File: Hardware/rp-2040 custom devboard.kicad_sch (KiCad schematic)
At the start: 36 parts, among them J1 USB_C_Receptacle_USB2.0_14P, J2 Conn_01x20, J3 Conn_01x20, J4 Conn_01x03, SW1 SW_Push, U1 RP2040, U2 MCP1700x-330xxTT, U3 W25Q128JVS, U4 SK6812MINI-E, Y1 12 MHz

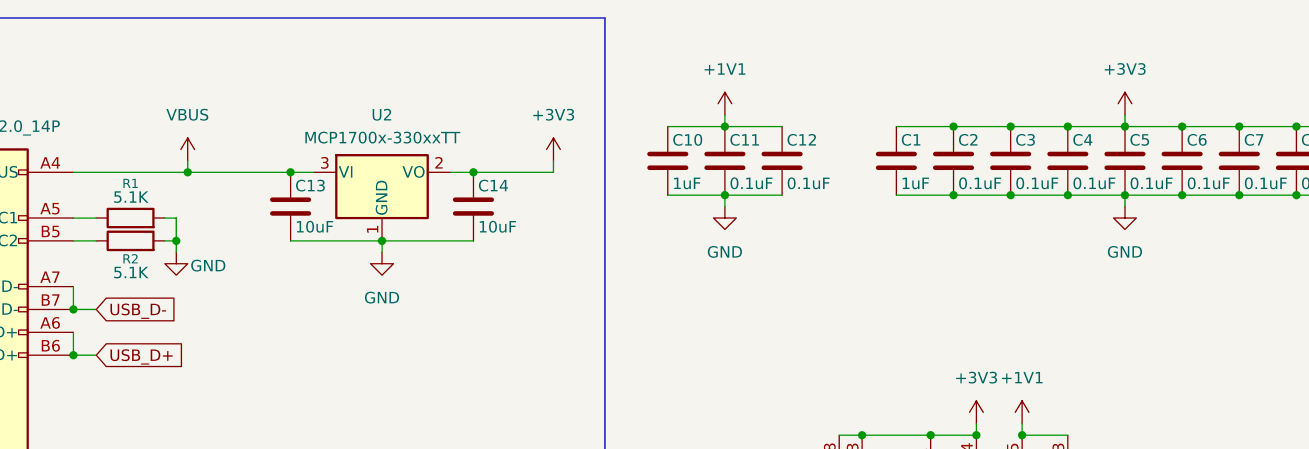
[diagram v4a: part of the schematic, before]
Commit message: learnt what PWR_FLAGs are and used them to get 0 ERC errors, lets go ahead with the footprints
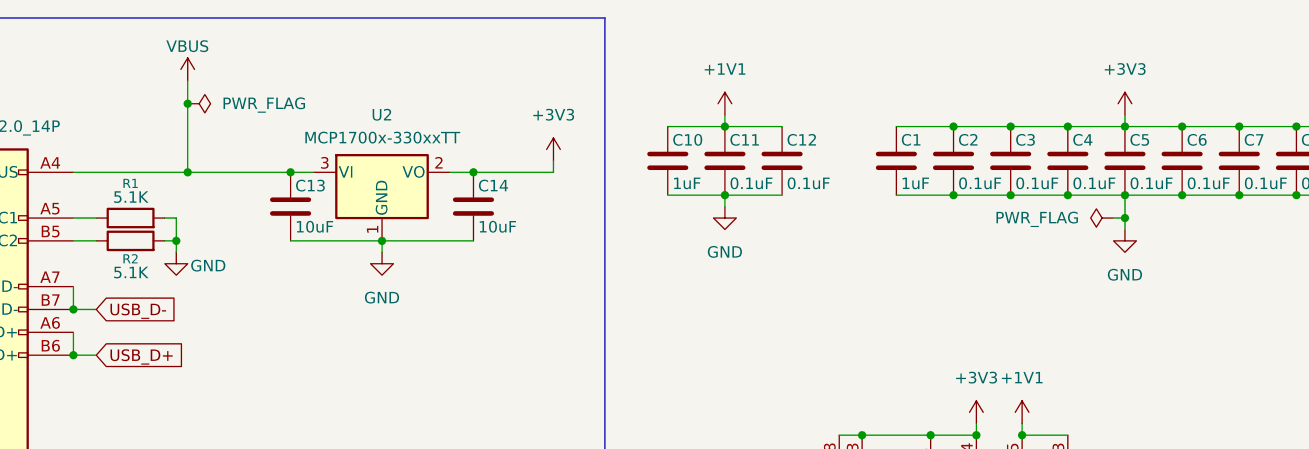
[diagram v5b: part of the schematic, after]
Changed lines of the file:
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@@
 	)
 	(junction
+		(at 64.77 25.4)
+		(diameter 0)
+		(color 0 0 0 0)
+	)
+	(junction
 		(at 256.54 43.18)
 		(diameter 0)
@@
 	)
 	(junction
+		(at 168.91 38.1)
+		(diameter 0)
+		(color 0 0 0 0)
+	)
+	(junction
 		(at 241.3 132.08)
 		(diameter 0)
@@
 	(wire
 		(pts
+			(xy 167.64 38.1) (xy 168.91 38.1)
+		)
+		(stroke
+			(width 0)
+			(type default)
+		)
+	)
+	(wire
+		(pts
 			(xy 80.01 163.83) (xy 80.01 176.53)
 		)
@@
 	(wire
 		(pts
-			(xy 64.77 31.75) (xy 64.77 33.02)
-		)
-		(stroke
-			(width 0)
-			(type default)
-		)
-	)
-	(wire
-		(pts
 			(xy 78.74 158.75) (xy 82.55 158.75)
 		)
@@
 	(wire
 		(pts
+			(xy 168.91 39.37) (xy 168.91 38.1)
+		)
+		(stroke
+			(width 0)
+			(type default)
+		)
+	)
+	(wire
+		(pts
 			(xy 168.91 26.67) (xy 168.91 27.94)
 		)
@@
 	(wire
 		(pts
+			(xy 64.77 25.4) (xy 64.77 33.02)
+		)
+		(stroke
+			(width 0)
+			(type default)
+		)
+	)
+	(wire
+		(pts
 			(xy 66.04 105.41) (xy 66.04 107.95)
 		)
@@
 	(wire
 		(pts
+			(xy 168.91 35.56) (xy 168.91 38.1)
+		)
+		(stroke
+			(width 0)
+			(type default)
+		)
+	)
+	(wire
+		(pts
 			(xy 175.26 146.05) (xy 176.53 146.05)
 		)
@@
 	(wire
 		(pts
-			(xy 168.91 35.56) (xy 168.91 36.83)
-		)
-		(stroke
-			(width 0)
-			(type default)
-		)
-	)
-	(wire
-		(pts
 			(xy 78.74 161.29) (xy 82.55 161.29)
 		)
@@
 	(wire
 		(pts
+			(xy 64.77 22.86) (xy 64.77 25.4)
+		)
+		(stroke
+			(width 0)
+			(type default)
+		)
+	)
+	(wire
+		(pts
 			(xy 139.7 62.23) (xy 147.32 62.23)
 		)
@@
 	)
 	(symbol
+		(lib_id "power:PWR_FLAG")
+		(at 64.77 25.4 270)
+		(unit 1)
+		(exclude_from_sim no)
+		(in_bom yes)
+		(on_board yes)
+		(dnp no)
+		(property "Reference" "#FLG02"
+			(at 66.675 25.4 0)
+			(effects
+				(font
+					(size 1.27 1.27)
+				)
+				(hide yes)
+			)
+		)
+		(property "Value" "PWR_FLAG"
+			(at 68.58 25.4001 90)
+			(effects
+				(font
+					(size 1.27 1.27)
+				)
+				(justify left)
+			)
+		)
+		(property "Footprint" ""
+			(at 64.77 25.4 0)
+			(effects
+				(font
+					(size 1.27 1.27)
+				)
+				(hide yes)
+			)
+		)
+		(property "Datasheet" "~"
+			(at 64.77 25.4 0)
+			(effects
+				(font
+					(size 1.27 1.27)
+				)
+				(hide yes)
+			)
+		)
+		(property "Description" "Special symbol for telling ERC where power comes from"
+			(at 64.77 25.4 0)
+			(effects
+				(font
+					(size 1.27 1.27)
+				)
+				(hide yes)
+			)
+		)
+		(pin "1"
+		)
+		(instances
+			(project ""
+				(path "/6a6cd6ef-7cbc-401d-a6e8-493482b4d165"
+					(reference "#FLG02")
+					(unit 1)
+				)
+			)
+		)
+	)
+	(symbol
 		(lib_id "Device:C")
 		(at 118.11 31.75 0)
@@
 	(symbol
 		(lib_id "power:GND")
-		(at 168.91 36.83 0)
+		(at 168.91 39.37 0)
 		(unit 1)
 		(exclude_from_sim no)
@@
 		(fields_autoplaced yes)
 		(property "Reference" "#PWR04"
-			(at 168.91 43.18 0)
+			(at 168.91 45.72 0)
 			(effects
 				(font
@@
 		)
 		(property "Value" "GND"
-			(at 168.91 41.91 0)
+			(at 168.91 44.45 0)
 			(effects
 				(font
@@
 		)
 		(property "Footprint" ""
-			(at 168.91 36.83 0)
+			(at 168.91 39.37 0)
 			(effects
 				(font
@@
 		)
 		(property "Datasheet" ""
-			(at 168.91 36.83 0)
+			(at 168.91 39.37 0)
 			(effects
 				(font
@@
 		)
 		(property "Description" "Power symbol creates a global label with name \"GND\" , ground"
-			(at 168.91 36.83 0)
+			(at 168.91 39.37 0)
 			(effects
 				(font
@@
 	(symbol
 		(lib_id "power:VBUS")
-		(at 64.77 31.75 0)
+		(at 64.77 22.86 0)
 		(unit 1)
 		(exclude_from_sim no)
@@
 		(fields_autoplaced yes)
 		(property "Reference" "#PWR010"
-			(at 64.77 35.56 0)
+			(at 64.77 26.67 0)
 			(effects
 				(font
@@
 		)
 		(property "Value" "VBUS"
-			(at 64.77 26.67 0)
+			(at 64.77 19.05 0)
 			(effects
 				(font
@@
 		)
 		(property "Footprint" ""
-			(at 64.77 31.75 0)
+			(at 64.77 22.86 0)
 			(effects
 				(font
@@
 		)
 		(property "Datasheet" ""
-			(at 64.77 31.75 0)
+			(at 64.77 22.86 0)
 			(effects
 				(font
@@
 		)
 		(property "Description" "Power symbol creates a global label with name \"VBUS\""
-			(at 64.77 31.75 0)
+			(at 64.77 22.86 0)
 			(effects
 				(font
@@
 					(unit 1)
 				)
+			)
+		)
+	)
+	(symbol
+		(lib_id "power:PWR_FLAG")
+		(at 167.64 38.1 90)
+		(unit 1)
+		(exclude_from_sim no)
+		(in_bom yes)
+		(on_board yes)
+		(dnp no)
+		(fields_autoplaced yes)
+		(property "Reference" "#FLG01"
+			(at 165.735 38.1 0)
+			(effects
+				(font
+					(size 1.27 1.27)
+				)
+				(hide yes)
+			)
+		)
+		(property "Value" "PWR_FLAG"
+			(at 163.83 38.0999 90)
+			(effects
+				(font
+					(size 1.27 1.27)
+				)
+				(justify left)
+			)
+		)
+		(property "Footprint" ""
+			(at 167.64 38.1 0)
+			(effects
+				(font
+					(size 1.27 1.27)
+				)
+				(hide yes)
+			)
+		)
+		(property "Datasheet" "~"
+			(at 167.64 38.1 0)
+			(effects
+				(font
+					(size 1.27 1.27)
+				)
+				(hide yes)
+			)
+		)
+		(property "Description" "Special symbol for telling ERC where power comes from"
+			(at 167.64 38.1 0)
+			(effects
+				(font
+					(size 1.27 1.27)
+				)
+				(hide yes)
+			)
+		)
+		(pin "1"
+		)
+		(instances
+			(project ""
+				(path "/6a6cd6ef-7cbc-401d-a6e8-493482b4d165"
+					(reference "#FLG01")
+					(unit 1)
+				)

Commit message: couldnt find the footprint for the SK6812MINI-E but i downloaded it again and it worked this time
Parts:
- C1, C10, C11, C12, C15, C16, C17, C2, C3, C4, C5, C6, C7, C8, C9: footprint (none) -> Capacitor_SMD:C_0402_1005Metric
- C13, C14: footprint (none) -> Capacitor_SMD:C_0603_1608Metric
- C19: value 100nF -> 0.1uF; footprint (none) -> Capacitor_SMD:C_0402_1005Metric
- J1: footprint (none) -> Connector_USB:USB_C_Receptacle_HRO_TYPE-C-31-M-12
- J2, J3: footprint (none) -> Connector_PinHeader_2.54mm:PinHeader_1x20_P2.54mm_Vertical
- J4: footprint (none) -> Connector_PinHeader_2.54mm:PinHeader_1x03_P2.54mm_Vertical
- R1, R2, R3, R4, R5, R6, R7, R9: footprint (none) -> Resistor_SMD:R_0402_1005Metric
- SW1: footprint (none) -> Button_Switch_SMD:SW_Push_SPST_NO_Alps_SKRK
- U4, Y1: footprint (none) -> Crystal:Crystal_SMD_3225-4Pin_3.2x2.5mm
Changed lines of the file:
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@@
 			)
 		)
-		(property "Footprint" ""
+		(property "Footprint" "Connector_PinHeader_2.54mm:PinHeader_1x20_P2.54mm_Vertical"
 			(at 43.18 156.21 0)
 			(effects
@@
 			)
 		)
-		(property "Footprint" ""
+		(property "Footprint" "Crystal:Crystal_SMD_3225-4Pin_3.2x2.5mm"
 			(at 49.53 102.87 0)
 			(effects
@@
 			)
 		)
-		(property "Footprint" ""
+		(property "Footprint" "Resistor_SMD:R_0402_1005Metric"
 			(at 119.38 94.488 90)
 			(effects
@@
 			)
 		)
-		(property "Footprint" ""
+		(property "Footprint" "Connector_USB:USB_C_Receptacle_HRO_TYPE-C-31-M-12"
 			(at 40.64 48.26 0)
 			(effects
@@
 			)
 		)
-		(property "Footprint" ""
+		(property "Footprint" "Capacitor_SMD:C_0402_1005Metric"
 			(at 176.2252 35.56 0)
 			(effects
@@
 			)
 		)
-		(property "Footprint" ""
+		(property "Footprint" "Resistor_SMD:R_0402_1005Metric"
 			(at 254 133.858 90)
 			(effects
@@
 			)
 		)
-		(property "Footprint" ""
+		(property "Footprint" "Capacitor_SMD:C_0402_1005Metric"
 			(at 131.7752 35.56 0)
 			(effects
@@
 			)
 		)
-		(property "Footprint" ""
+		(property "Footprint" "Capacitor_SMD:C_0402_1005Metric"
 			(at 233.68 120.9548 0)
 			(effects
@@
 			)
 		)
-		(property "Footprint" ""
+		(property "Footprint" "Capacitor_SMD:C_0402_1005Metric"
 			(at 195.2752 35.56 0)
 			(effects
@@
 			)
 		)
-		(property "Footprint" ""
+		(property "Footprint" "Capacitor_SMD:C_0402_1005Metric"
 			(at 188.9252 35.56 0)
 			(effects
@@
 			)
 		)
-		(property "Footprint" ""
+		(property "Footprint" "Capacitor_SMD:C_0402_1005Metric"
 			(at 150.8252 35.56 0)
 			(effects
@@
 			)
 		)
-		(property "Footprint" ""
+		(property "Footprint" "Capacitor_SMD:C_0402_1005Metric"
 			(at 144.4752 35.56 0)
 			(effects
@@
 			)
 		)
-		(property "Footprint" ""
+		(property "Footprint" "Crystal:Crystal_SMD_3225-4Pin_3.2x2.5mm"
 			(at 241.3 127 0)
 			(effects
@@
 			)
 		)
-		(property "Footprint" ""
+		(property "Footprint" "Capacitor_SMD:C_0402_1005Metric"
 			(at 119.0752 35.56 0)
 			(effects
@@
 			)
 		)
-		(property "Footprint" ""
+		(property "Footprint" "Resistor_SMD:R_0402_1005Metric"
 			(at 228.6 56.388 90)
 			(effects
@@
 			)
 		)
-		(property "Footprint" ""
+		(property "Footprint" "Resistor_SMD:R_0402_1005Metric"
 			(at 58.42 39.878 90)
 			(effects
@@
 			)
 		)
-		(property "Footprint" ""
+		(property "Footprint" "Capacitor_SMD:C_0402_1005Metric"
 			(at 182.5752 35.56 0)
 			(effects
@@
 			)
 		)
-		(property "Footprint" ""
+		(property "Footprint" "Capacitor_SMD:C_0402_1005Metric"
 			(at 157.1752 35.56 0)
 			(effects
@@
 			)
 		)
-		(property "Footprint" ""
+		(property "Footprint" "Capacitor_SMD:C_0402_1005Metric"
 			(at 233.68 131.1148 0)
 			(effects
@@
 			)
 		)
-		(property "Footprint" ""
+		(property "Footprint" "Capacitor_SMD:C_0603_1608Metric"
 			(at 97.4852 40.64 0)
 			(effects
@@
 			)
 		)
-		(property "Footprint" ""
+		(property "Footprint" "Capacitor_SMD:C_0402_1005Metric"
 			(at 163.5252 35.56 0)
 			(effects
@@
 			)
 		)
-		(property "Footprint" ""
+		(property "Footprint" "Resistor_SMD:R_0402_1005Metric"
 			(at 237.998 49.53 90)
 			(effects
@@
 			)
 		)
-		(property "Footprint" ""
+		(property "Footprint" "Resistor_SMD:R_0402_1005Metric"
 			(at 69.85 101.092 90)
 			(effects
@@
 		(fields_autoplaced yes)
 		(property "Reference" "C19"
-			(at 33.528 95.504 0)
+			(at 33.528 95.25 0)
 			(effects
 				(font
@@
 			)
 		)
-		(property "Value" "100nF"
-			(at 33.528 100.076 0)
+		(property "Value" "0.1uF"
+			(at 33.528 100.584 0)
 			(effects
 				(font
@@
 			)
 		)
-		(property "Footprint" ""
+		(property "Footprint" "Capacitor_SMD:C_0402_1005Metric"
 			(at 33.9852 101.6 0)
 			(effects
@@
 			)
 		)
-		(property "Footprint" ""
+		(property "Footprint" "Capacitor_SMD:C_0402_1005Metric"
 			(at 169.8752 35.56 0)
 			(effects
@@
 			)
 		)
-		(property "Footprint" ""
+		(property "Footprint" "Resistor_SMD:R_0402_1005Metric"
 			(at 58.42 42.418 90)
 			(effects
@@
 			)
 		)
-		(property "Footprint" ""
+		(property "Footprint" "Button_Switch_SMD:SW_Push_SPST_NO_Alps_SKRK"
 			(at 217.17 49.53 0)
 			(effects
@@
 			)
 		)
-		(property "Footprint" ""
+		(property "Footprint" "Capacitor_SMD:C_0402_1005Metric"
 			(at 257.81 44.1452 0)
 			(effects
@@
 			)
 		)
-		(property "Footprint" ""
+		(property "Footprint" "Connector_PinHeader_2.54mm:PinHeader_1x20_P2.54mm_Vertical"
 			(at 73.66 156.21 0)
 			(effects
@@
 			)
 		)
-		(property "Footprint" ""
+		(property "Footprint" "Resistor_SMD:R_0402_1005Metric"
 			(at 119.38 97.028 90)
 			(effects
@@
 			)
 		)
-		(property "Footprint" ""
+		(property "Footprint" "Capacitor_SMD:C_0603_1608Metric"
 			(at 77.1652 40.64 0)
 			(effects
@@
 			)
 		)
-		(property "Footprint" ""
+		(property "Footprint" "Connector_PinHeader_2.54mm:PinHeader_1x03_P2.54mm_Vertical"
 			(at 58.42 182.88 0)
 			(effects
@@
 			)
 		)
-		(property "Footprint" ""
+		(property "Footprint" "Capacitor_SMD:C_0402_1005Metric"
 			(at 125.4252 35.56 0)
 			(effects
